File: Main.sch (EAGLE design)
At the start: 11 parts, among them U2 LM 1084 IT5,0, U3 LM 1084 IT3,3, X1 12V

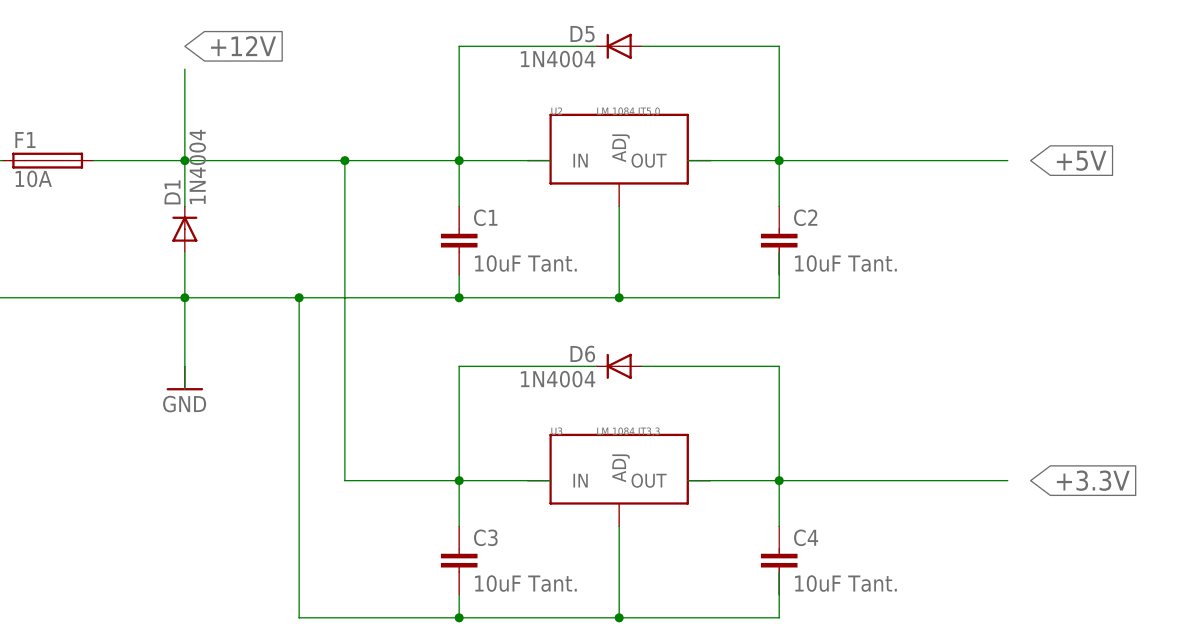
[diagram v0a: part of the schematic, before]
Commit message: fixed it... misleading warnings due to unneeded wires
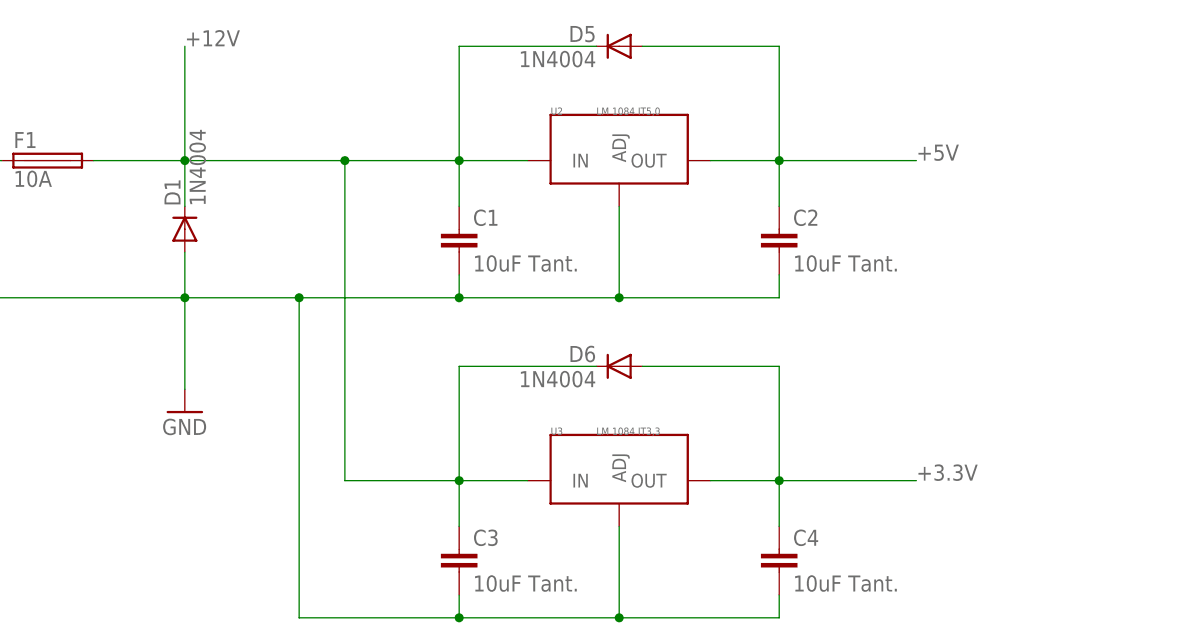
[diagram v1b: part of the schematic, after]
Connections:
- net N$3 renamed GND
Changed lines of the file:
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@@
 <part name="C3" library="rcl" deviceset="C-EU" device="025-040X050" value="10uF Tant."/>
 <part name="C4" library="rcl" deviceset="C-EU" device="025-040X050" value="10uF Tant."/>
-<part name="FRAME2" library="frames" deviceset="DINA4_L" device=""/>
-<part name="GND1" library="supply1" deviceset="GND" device=""/>
 <part name="D1" library="diode" deviceset="1N4004" device=""/>
 <part name="F1" library="fuse" deviceset="FUSE" device="BLANK_5X20MM" value="10A"/>
+<part name="GND1" library="supply1" deviceset="GND" device=""/>
 </parts>
 <sheets>
@@
 <instance part="C3" gate="G$1" x="-429.26" y="297.18"/>
 <instance part="C4" gate="G$1" x="-393.7" y="297.18"/>
-<instance part="FRAME2" gate="G$1" x="-502.92" y="27.94"/>
-<instance part="FRAME2" gate="G$2" x="-340.36" y="27.94"/>
-<instance part="GND1" gate="1" x="-459.74" y="314.96"/>
 <instance part="D1" gate="1" x="-459.74" y="332.74" rot="R90"/>
 <instance part="F1" gate="G$1" x="-474.98" y="340.36"/>
+<instance part="GND1" gate="1" x="-459.74" y="312.42"/>
 </instances>
 <busses>
@@
 <wire x1="-393.7" y1="353.06" x2="-393.7" y2="340.36" width="0.1524" layer="91"/>
 <wire x1="-393.7" y1="340.36" x2="-393.7" y2="335.28" width="0.1524" layer="91"/>
-<wire x1="-403.86" y1="340.36" x2="-401.32" y2="340.36" width="0.1524" layer="91"/>
 <junction x="-393.7" y="340.36"/>
+<wire x1="-393.7" y1="340.36" x2="-378.46" y2="340.36" width="0.1524" layer="91"/>
+<label x="-378.46" y="340.36" size="1.778" layer="95"/>
 <pinref part="U2" gate="G$1" pin="OUT"/>
-<wire x1="-401.32" y1="340.36" x2="-393.7" y2="340.36" width="0.1524" layer="91"/>
-<wire x1="-393.7" y1="340.36" x2="-368.3" y2="340.36" width="0.1524" layer="91"/>
-<label x="-365.76" y="340.36" size="2.1844" layer="95" xref="yes"/>
+<wire x1="-393.7" y1="340.36" x2="-401.32" y2="340.36" width="0.1524" layer="91"/>
 </segment>
 </net>
@@
 <wire x1="-393.7" y1="317.5" x2="-393.7" y2="304.8" width="0.1524" layer="91"/>
 <wire x1="-393.7" y1="304.8" x2="-393.7" y2="299.72" width="0.1524" layer="91"/>
-<wire x1="-403.86" y1="304.8" x2="-401.32" y2="304.8" width="0.1524" layer="91"/>
 <junction x="-393.7" y="304.8"/>
+<wire x1="-393.7" y1="304.8" x2="-378.46" y2="304.8" width="0.1524" layer="91"/>
+<label x="-378.46" y="304.8" size="1.778" layer="95"/>
 <pinref part="U3" gate="G$1" pin="OUT"/>
 <wire x1="-401.32" y1="304.8" x2="-393.7" y2="304.8" width="0.1524" layer="91"/>
-<wire x1="-393.7" y1="304.8" x2="-368.3" y2="304.8" width="0.1524" layer="91"/>
-<label x="-365.76" y="304.8" size="2.1844" layer="95" xref="yes"/>
 </segment>
 </net>
@@
 <segment>
 <wire x1="-429.26" y1="304.8" x2="-421.64" y2="304.8" width="0.1524" layer="91"/>
-<wire x1="-421.64" y1="304.8" x2="-419.1" y2="304.8" width="0.1524" layer="91"/>
 <junction x="-429.26" y="304.8"/>
 <wire x1="-429.26" y1="299.72" x2="-429.26" y2="304.8" width="0.1524" layer="91"/>
@@
 <wire x1="-429.26" y1="304.8" x2="-441.96" y2="304.8" width="0.1524" layer="91"/>
 <wire x1="-429.26" y1="340.36" x2="-421.64" y2="340.36" width="0.1524" layer="91"/>
-<wire x1="-421.64" y1="340.36" x2="-419.1" y2="340.36" width="0.1524" layer="91"/>
 <junction x="-429.26" y="340.36"/>
 <wire x1="-429.26" y1="335.28" x2="-429.26" y2="340.36" width="0.1524" layer="91"/>
@@
 <junction x="-441.96" y="340.36"/>
 <wire x1="-459.74" y1="340.36" x2="-441.96" y2="340.36" width="0.1524" layer="91"/>
-<wire x1="-459.74" y1="340.36" x2="-459.74" y2="350.52" width="0.1524" layer="91"/>
-<label x="-459.74" y="353.06" size="2.1844" layer="95" xref="yes"/>
 <pinref part="D1" gate="1" pin="C"/>
 <wire x1="-459.74" y1="340.36" x2="-459.74" y2="335.28" width="0.1524" layer="91"/>
@@
 <pinref part="F1" gate="G$1" pin="2"/>
 <wire x1="-469.9" y1="340.36" x2="-459.74" y2="340.36" width="0.1524" layer="91"/>
-</segment>
-</net>
-<net name="N$3" class="0">
-<segment>
-<wire x1="-429.26" y1="289.56" x2="-411.48" y2="289.56" width="0.1524" layer="91"/>
-<wire x1="-411.48" y1="289.56" x2="-393.7" y2="289.56" width="0.1524" layer="91"/>
-<wire x1="-393.7" y1="289.56" x2="-393.7" y2="292.1" width="0.1524" layer="91"/>
-<pinref part="C3" gate="G$1" pin="2"/>
-<wire x1="-393.7" y1="292.1" x2="-393.7" y2="294.64" width="0.1524" layer="91"/>
-<wire x1="-429.26" y1="292.1" x2="-429.26" y2="289.56" width="0.1524" layer="91"/>
-<pinref part="U3" gate="G$1" pin="ADJ"/>
-<wire x1="-411.48" y1="299.72" x2="-411.48" y2="289.56" width="0.1524" layer="91"/>
-<junction x="-411.48" y="289.56"/>
-<pinref part="C4" gate="G$1" pin="2"/>
-<wire x1="-429.26" y1="325.12" x2="-411.48" y2="325.12" width="0.1524" layer="91"/>
-<wire x1="-411.48" y1="325.12" x2="-393.7" y2="325.12" width="0.1524" layer="91"/>
-<wire x1="-393.7" y1="325.12" x2="-393.7" y2="327.66" width="0.1524" layer="91"/>
-<pinref part="C1" gate="G$1" pin="2"/>
-<wire x1="-393.7" y1="327.66" x2="-393.7" y2="330.2" width="0.1524" layer="91"/>
-<wire x1="-429.26" y1="327.66" x2="-429.26" y2="325.12" width="0.1524" layer="91"/>
-<pinref part="U2" gate="G$1" pin="ADJ"/>
-<wire x1="-411.48" y1="335.28" x2="-411.48" y2="325.12" width="0.1524" layer="91"/>
-<junction x="-411.48" y="325.12"/>
-<pinref part="C2" gate="G$1" pin="2"/>
-<junction x="-429.26" y="325.12"/>
-<wire x1="-447.04" y1="325.12" x2="-429.26" y2="325.12" width="0.1524" layer="91"/>
-<wire x1="-429.26" y1="289.56" x2="-447.04" y2="289.56" width="0.1524" layer="91"/>
-<wire x1="-447.04" y1="289.56" x2="-447.04" y2="325.12" width="0.1524" layer="91"/>
-<junction x="-429.26" y="289.56"/>
-<junction x="-447.04" y="325.12"/>
-<wire x1="-459.74" y1="325.12" x2="-447.04" y2="325.12" width="0.1524" layer="91"/>
-<wire x1="-459.74" y1="314.96" x2="-459.74" y2="325.12" width="0.1524" layer="91"/>
-<pinref part="D1" gate="1" pin="A"/>
-<wire x1="-459.74" y1="325.12" x2="-459.74" y2="330.2" width="0.1524" layer="91"/>
-<junction x="-459.74" y="325.12"/>
-<pinref part="X1" gate="-2" pin="KL"/>
-<wire x1="-487.68" y1="325.12" x2="-459.74" y2="325.12" width="0.1524" layer="91"/>
+<wire x1="-459.74" y1="340.36" x2="-459.74" y2="353.06" width="0.1524" layer="91"/>
+<label x="-459.74" y="353.06" size="1.778" layer="95"/>
 </segment>
 </net>
@@
 </segment>
 </net>
+<net name="GND" class="0">
+<segment>
+<wire x1="-429.26" y1="289.56" x2="-411.48" y2="289.56" width="0.1524" layer="91"/>
+<wire x1="-411.48" y1="289.56" x2="-393.7" y2="289.56" width="0.1524" layer="91"/>
+<pinref part="C3" gate="G$1" pin="2"/>
+<wire x1="-429.26" y1="292.1" x2="-429.26" y2="289.56" width="0.1524" layer="91"/>
+<pinref part="U3" gate="G$1" pin="ADJ"/>
+<wire x1="-411.48" y1="299.72" x2="-411.48" y2="289.56" width="0.1524" layer="91"/>
+<junction x="-411.48" y="289.56"/>
+<wire x1="-429.26" y1="325.12" x2="-411.48" y2="325.12" width="0.1524" layer="91"/>
+<wire x1="-411.48" y1="325.12" x2="-393.7" y2="325.12" width="0.1524" layer="91"/>
+<pinref part="C1" gate="G$1" pin="2"/>
+<wire x1="-429.26" y1="327.66" x2="-429.26" y2="325.12" width="0.1524" layer="91"/>
+<pinref part="U2" gate="G$1" pin="ADJ"/>
+<wire x1="-411.48" y1="335.28" x2="-411.48" y2="325.12" width="0.1524" layer="91"/>
+<junction x="-411.48" y="325.12"/>
+<junction x="-429.26" y="325.12"/>
+<wire x1="-447.04" y1="325.12" x2="-429.26" y2="325.12" width="0.1524" layer="91"/>
+<wire x1="-429.26" y1="289.56" x2="-447.04" y2="289.56" width="0.1524" layer="91"/>
+<wire x1="-447.04" y1="289.56" x2="-447.04" y2="325.12" width="0.1524" layer="91"/>
+<junction x="-429.26" y="289.56"/>
+<junction x="-447.04" y="325.12"/>
+<pinref part="X1" gate="-2" pin="KL"/>
+<wire x1="-487.68" y1="325.12" x2="-459.74" y2="325.12" width="0.1524" layer="91"/>
+<pinref part="C2" gate="G$1" pin="2"/>
+<wire x1="-459.74" y1="325.12" x2="-447.04" y2="325.12" width="0.1524" layer="91"/>
+<wire x1="-393.7" y1="327.66" x2="-393.7" y2="325.12" width="0.1524" layer="91"/>
+<pinref part="C4" gate="G$1" pin="2"/>
+<wire x1="-393.7" y1="289.56" x2="-393.7" y2="292.1" width="0.1524" layer="91"/>
+<junction x="-459.74" y="325.12"/>
+<pinref part="D1" gate="1" pin="A"/>
+<wire x1="-459.74" y1="325.12" x2="-459.74" y2="330.2" width="0.1524" layer="91"/>
+<pinref part="GND1" gate="1" pin="GND"/>
+<wire x1="-459.74" y1="314.96" x2="-459.74" y2="325.12" width="0.1524" layer="91"/>
+</segment>
+</net>

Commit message: got rid of hopefully redundant C
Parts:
- removed C3: 10uF Tant., rcl:C-EU025-040X050
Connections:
- net +12V: no longer C3.1
- net GND: no longer C3.2
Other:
- moved on the sheet: C1
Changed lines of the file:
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@@
 <part name="U3" library="PP_PowerIC" deviceset="LM1084" device="TO-263-3" value="LM 1084 IT3,3"/>
 <part name="D6" library="diode" deviceset="1N4004" device=""/>
-<part name="C3" library="rcl" deviceset="C-EU" device="025-040X050" value="10uF Tant."/>
 <part name="C4" library="rcl" deviceset="C-EU" device="025-040X050" value="10uF Tant."/>
 <part name="D1" library="diode" deviceset="1N4004" device=""/>
@@
 <instance part="U2" gate="G$1" x="-411.48" y="340.36"/>
 <instance part="D5" gate="1" x="-411.48" y="353.06" rot="MR0"/>
-<instance part="C1" gate="G$1" x="-429.26" y="332.74"/>
+<instance part="C1" gate="G$1" x="-452.12" y="332.74"/>
 <instance part="C2" gate="G$1" x="-393.7" y="332.74"/>
 <instance part="FRAME1" gate="G$1" x="-502.92" y="215.9"/>
@@
 <instance part="U3" gate="G$1" x="-411.48" y="304.8"/>
 <instance part="D6" gate="1" x="-411.48" y="317.5" rot="MR0"/>
-<instance part="C3" gate="G$1" x="-429.26" y="297.18"/>
 <instance part="C4" gate="G$1" x="-393.7" y="297.18"/>
 <instance part="D1" gate="1" x="-459.74" y="332.74" rot="R90"/>
@@
 <wire x1="-429.26" y1="304.8" x2="-421.64" y2="304.8" width="0.1524" layer="91"/>
 <junction x="-429.26" y="304.8"/>
-<wire x1="-429.26" y1="299.72" x2="-429.26" y2="304.8" width="0.1524" layer="91"/>
 <wire x1="-429.26" y1="304.8" x2="-429.26" y2="317.5" width="0.1524" layer="91"/>
 <pinref part="D6" gate="1" pin="C"/>
 <wire x1="-429.26" y1="317.5" x2="-414.02" y2="317.5" width="0.1524" layer="91"/>
 <pinref part="U3" gate="G$1" pin="IN"/>
-<pinref part="C3" gate="G$1" pin="1"/>
 <wire x1="-429.26" y1="304.8" x2="-441.96" y2="304.8" width="0.1524" layer="91"/>
 <wire x1="-429.26" y1="340.36" x2="-421.64" y2="340.36" width="0.1524" layer="91"/>
 <junction x="-429.26" y="340.36"/>
-<wire x1="-429.26" y1="335.28" x2="-429.26" y2="340.36" width="0.1524" layer="91"/>
 <wire x1="-429.26" y1="340.36" x2="-429.26" y2="353.06" width="0.1524" layer="91"/>
 <pinref part="D5" gate="1" pin="C"/>
 <wire x1="-429.26" y1="353.06" x2="-414.02" y2="353.06" width="0.1524" layer="91"/>
 <pinref part="U2" gate="G$1" pin="IN"/>
-<pinref part="C1" gate="G$1" pin="1"/>
 <wire x1="-441.96" y1="340.36" x2="-429.26" y2="340.36" width="0.1524" layer="91"/>
 <wire x1="-441.96" y1="304.8" x2="-441.96" y2="340.36" width="0.1524" layer="91"/>
 <junction x="-441.96" y="340.36"/>
-<wire x1="-459.74" y1="340.36" x2="-441.96" y2="340.36" width="0.1524" layer="91"/>
+<wire x1="-459.74" y1="340.36" x2="-452.12" y2="340.36" width="0.1524" layer="91"/>
 <pinref part="D1" gate="1" pin="C"/>
+<wire x1="-452.12" y1="340.36" x2="-441.96" y2="340.36" width="0.1524" layer="91"/>
 <wire x1="-459.74" y1="340.36" x2="-459.74" y2="335.28" width="0.1524" layer="91"/>
 <junction x="-459.74" y="340.36"/>
@@
 <wire x1="-459.74" y1="340.36" x2="-459.74" y2="353.06" width="0.1524" layer="91"/>
 <label x="-459.74" y="353.06" size="1.778" layer="95"/>
+<pinref part="C1" gate="G$1" pin="1"/>
+<wire x1="-452.12" y1="335.28" x2="-452.12" y2="340.36" width="0.1524" layer="91"/>
+<junction x="-452.12" y="340.36"/>
 </segment>
 </net>
@@
 <net name="GND" class="0">
 <segment>
-<wire x1="-429.26" y1="289.56" x2="-411.48" y2="289.56" width="0.1524" layer="91"/>
 <wire x1="-411.48" y1="289.56" x2="-393.7" y2="289.56" width="0.1524" layer="91"/>
-<pinref part="C3" gate="G$1" pin="2"/>
-<wire x1="-429.26" y1="292.1" x2="-429.26" y2="289.56" width="0.1524" layer="91"/>
 <pinref part="U3" gate="G$1" pin="ADJ"/>
 <wire x1="-411.48" y1="299.72" x2="-411.48" y2="289.56" width="0.1524" layer="91"/>
 <junction x="-411.48" y="289.56"/>
-<wire x1="-429.26" y1="325.12" x2="-411.48" y2="325.12" width="0.1524" layer="91"/>
 <wire x1="-411.48" y1="325.12" x2="-393.7" y2="325.12" width="0.1524" layer="91"/>
-<pinref part="C1" gate="G$1" pin="2"/>
-<wire x1="-429.26" y1="327.66" x2="-429.26" y2="325.12" width="0.1524" layer="91"/>
 <pinref part="U2" gate="G$1" pin="ADJ"/>
 <wire x1="-411.48" y1="335.28" x2="-411.48" y2="325.12" width="0.1524" layer="91"/>
 <junction x="-411.48" y="325.12"/>
-<junction x="-429.26" y="325.12"/>
-<wire x1="-447.04" y1="325.12" x2="-429.26" y2="325.12" width="0.1524" layer="91"/>
-<wire x1="-429.26" y1="289.56" x2="-447.04" y2="289.56" width="0.1524" layer="91"/>
+<wire x1="-447.04" y1="325.12" x2="-411.48" y2="325.12" width="0.1524" layer="91"/>
+<wire x1="-411.48" y1="289.56" x2="-447.04" y2="289.56" width="0.1524" layer="91"/>
 <wire x1="-447.04" y1="289.56" x2="-447.04" y2="325.12" width="0.1524" layer="91"/>
-<junction x="-429.26" y="289.56"/>
 <junction x="-447.04" y="325.12"/>
 <pinref part="X1" gate="-2" pin="KL"/>
 <wire x1="-487.68" y1="325.12" x2="-459.74" y2="325.12" width="0.1524" layer="91"/>
 <pinref part="C2" gate="G$1" pin="2"/>
-<wire x1="-459.74" y1="325.12" x2="-447.04" y2="325.12" width="0.1524" layer="91"/>
+<wire x1="-459.74" y1="325.12" x2="-452.12" y2="325.12" width="0.1524" layer="91"/>
+<wire x1="-452.12" y1="325.12" x2="-447.04" y2="325.12" width="0.1524" layer="91"/>
 <wire x1="-393.7" y1="327.66" x2="-393.7" y2="325.12" width="0.1524" layer="91"/>
 <pinref part="C4" gate="G$1" pin="2"/>
@@
 <pinref part="GND1" gate="1" pin="GND"/>
 <wire x1="-459.74" y1="314.96" x2="-459.74" y2="325.12" width="0.1524" layer="91"/>
+<pinref part="C1" gate="G$1" pin="2"/>
+<wire x1="-452.12" y1="327.66" x2="-452.12" y2="325.12" width="0.1524" layer="91"/>
+<junction x="-452.12" y="325.12"/>
 </segment>
 </net>

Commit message: finally got connections without wires
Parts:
- added R1: 4711, resistor:R-EU_0617/22
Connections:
- net +12V: now also R1.1
- net GND: now also R1.2
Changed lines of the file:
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@@
 <part name="C1" library="rcl" deviceset="C-EU" device="025-040X050" value="10uF Tant."/>
 <part name="C2" library="rcl" deviceset="C-EU" device="025-040X050" value="10uF Tant."/>
-<part name="FRAME1" library="frames" deviceset="DINA4_L" device=""/>
 <part name="X1" library="con-wago-508" deviceset="W237-02P" device="" value="12V"/>
 <part name="U3" library="PP_PowerIC" deviceset="LM1084" device="TO-263-3" value="LM 1084 IT3,3"/>
@@
 <part name="D1" library="diode" deviceset="1N4004" device=""/>
 <part name="F1" library="fuse" deviceset="FUSE" device="BLANK_5X20MM" value="10A"/>
-<part name="GND1" library="supply1" deviceset="GND" device=""/>
+<part name="R1" library="resistor" deviceset="R-EU_" device="0617/22" value="4711"/>
+<part name="FRAME1" library="frames" deviceset="DINA4_L" device=""/>
 </parts>
 <sheets>
@@
 <instance part="C1" gate="G$1" x="-452.12" y="332.74"/>
 <instance part="C2" gate="G$1" x="-393.7" y="332.74"/>
-<instance part="FRAME1" gate="G$1" x="-502.92" y="215.9"/>
-<instance part="FRAME1" gate="G$2" x="-340.36" y="215.9"/>
 <instance part="X1" gate="-1" x="-492.76" y="340.36"/>
 <instance part="X1" gate="-2" x="-492.76" y="325.12"/>
@@
 <instance part="D1" gate="1" x="-459.74" y="332.74" rot="R90"/>
 <instance part="F1" gate="G$1" x="-474.98" y="340.36"/>
-<instance part="GND1" gate="1" x="-459.74" y="312.42"/>
+<instance part="R1" gate="G$1" x="-464.82" y="365.76"/>
+<instance part="FRAME1" gate="G$1" x="-513.08" y="213.36"/>
+<instance part="FRAME1" gate="G$2" x="-350.52" y="213.36"/>
 </instances>
 <busses>
@@
 <pinref part="F1" gate="G$1" pin="2"/>
 <wire x1="-469.9" y1="340.36" x2="-459.74" y2="340.36" width="0.1524" layer="91"/>
-<wire x1="-459.74" y1="340.36" x2="-459.74" y2="353.06" width="0.1524" layer="91"/>
-<label x="-459.74" y="353.06" size="1.778" layer="95"/>
 <pinref part="C1" gate="G$1" pin="1"/>
 <wire x1="-452.12" y1="335.28" x2="-452.12" y2="340.36" width="0.1524" layer="91"/>
 <junction x="-452.12" y="340.36"/>
+<wire x1="-459.74" y1="340.36" x2="-459.74" y2="350.52" width="0.1524" layer="91"/>
+<label x="-459.74" y="350.52" size="1.778" layer="95"/>
+</segment>
+<segment>
+<pinref part="R1" gate="G$1" pin="1"/>
+<wire x1="-469.9" y1="365.76" x2="-472.44" y2="365.76" width="0.1524" layer="91"/>
+<label x="-480.06" y="365.76" size="1.778" layer="95"/>
 </segment>
 </net>
@@
 <pinref part="D1" gate="1" pin="A"/>
 <wire x1="-459.74" y1="325.12" x2="-459.74" y2="330.2" width="0.1524" layer="91"/>
-<pinref part="GND1" gate="1" pin="GND"/>
-<wire x1="-459.74" y1="314.96" x2="-459.74" y2="325.12" width="0.1524" layer="91"/>
 <pinref part="C1" gate="G$1" pin="2"/>
 <wire x1="-452.12" y1="327.66" x2="-452.12" y2="325.12" width="0.1524" layer="91"/>
 <junction x="-452.12" y="325.12"/>
+<wire x1="-459.74" y1="325.12" x2="-459.74" y2="314.96" width="0.1524" layer="91"/>
+<label x="-459.74" y="314.96" size="1.778" layer="95"/>
+</segment>
+<segment>
+<pinref part="R1" gate="G$1" pin="2"/>
+<wire x1="-459.74" y1="365.76" x2="-457.2" y2="365.76" width="0.1524" layer="91"/>
+<label x="-454.66" y="365.76" size="1.778" layer="95"/>
 </segment>
 </net>
